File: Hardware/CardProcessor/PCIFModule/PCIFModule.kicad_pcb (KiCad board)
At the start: 8 copper layers, 144 x 70.5 mm, 31 parts, among them J1 MEC5-140-01-L-DV-W1-K, U4 74ABT32, U5 74AHCT04, U6 IDT7381, U8 74ABT16374, U9 74ABT16374

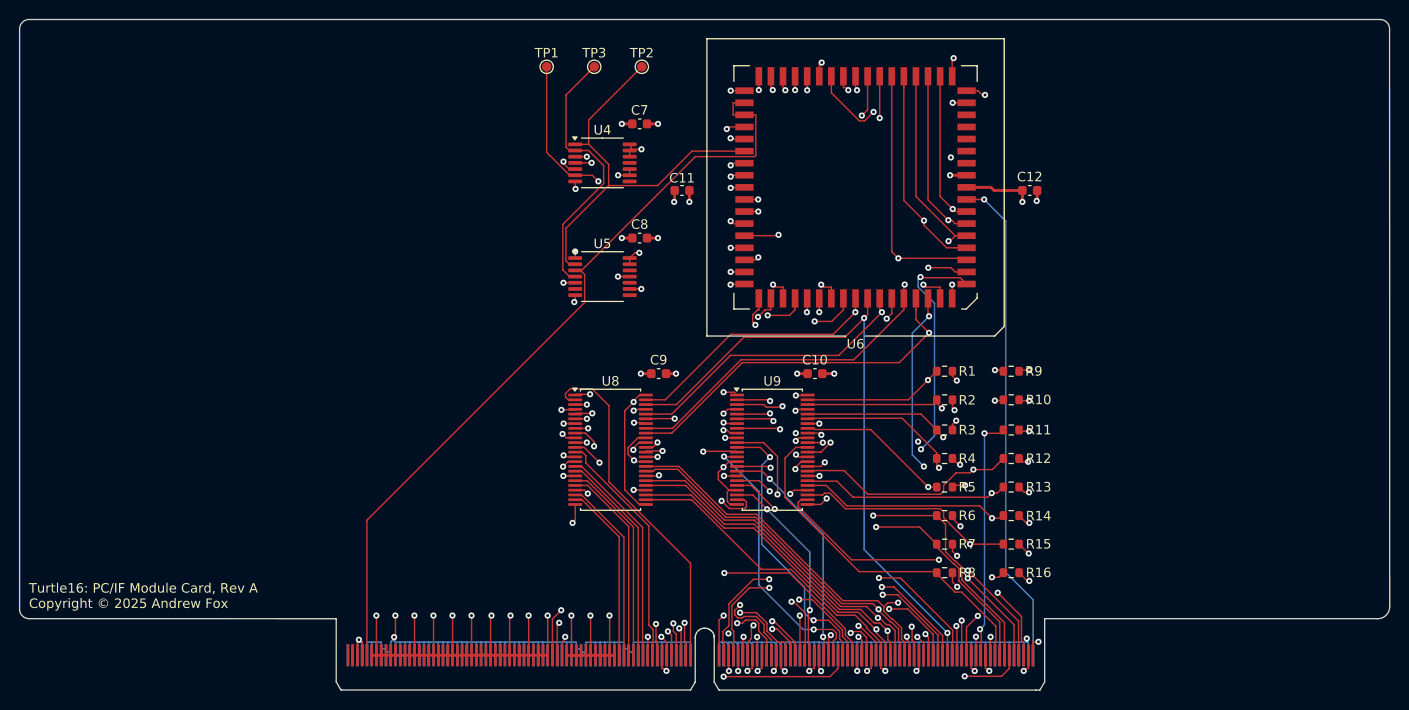
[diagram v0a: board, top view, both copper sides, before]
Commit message: PCIFModule: Route the PCB again, better
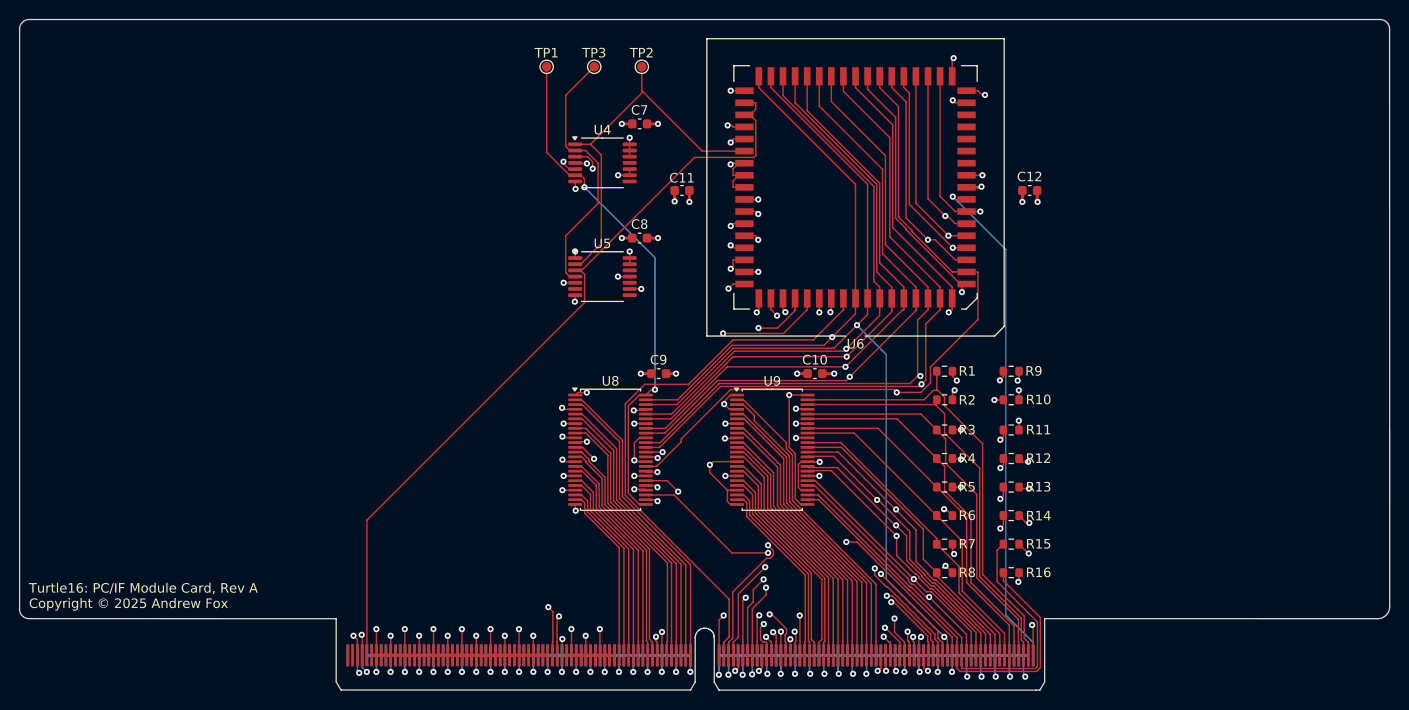
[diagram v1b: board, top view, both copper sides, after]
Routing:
- net GND: track 412.4 -> 314.8 mm, vias 62 -> 104
- net /CardEdgePCIF/Y_EX14: track 70.2 -> 42.7 mm
- net /IF/sheet5FE3DA15/PC5: track 112.5 -> 95.8 mm, vias 3 -> 2
- net /CardEdgePCIF/Ins_ID8: track 41.9 -> 26.2 mm, vias 2 -> 0
- net /CardEdgePCIF/Y_EX15: track 46.1 -> 59.4 mm, vias 2 -> 0
- net /CardEdgePCIF/Ins_IF14: track 35.5 -> 48.6 mm, vias 2 -> 0
- net /CardEdgePCIF/FLUSH_IF: track 96.2 -> 86.7 mm, vias 3 -> 2
- net /CardEdgePCIF/Y_EX3: track 57.4 -> 48.1 mm
- net /CardEdgePCIF/Ins_IF9: track 57.0 -> 48.1 mm, vias 3 -> 2
- net /CardEdgePCIF/Ins_IF15: track 37.2 -> 45.6 mm, vias 3 -> 0
- net /IF/sheet5FE3DA15/PC4: track 103.8 -> 95.6 mm, vias 3 -> 2
- net /CardEdgePCIF/Ins_IF0: track 55.5 -> 47.9 mm, vias 2 -> 0
- net /CardEdgePCIF/Ins_IF4: track 44.0 -> 37.0 mm, vias 2 -> 0
- net /CardEdgePCIF/Y_EX9: track 46.8 -> 39.8 mm
- net /CardEdgePCIF/Ins_ID5: track 35.5 -> 28.8 mm, vias 2 -> 0
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
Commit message: PCIFModule: route the six layer PCB
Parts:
- moved TP2 27.1 mm to (103.2, 63.0)
- moved TP3 23.4 mm to (103.2, 69.0)
- moved TP1 21.4 mm to (103.2, 74.0)
- moved C7 14.0 mm to (116.0, 67.0)
- moved C8 14.0 mm to (116.0, 79.0)
- moved C9 14.0 mm to (118.0, 93.2)
- moved U4 14.0 mm to (112.1, 71.1)
- moved U5 14.0 mm to (112.1, 83.0)
- moved U8 14.0 mm to (112.9, 101.2)
- moved U9 8.46 mm to (135.4, 101.2)
- moved C10 8.46 mm to (139.9, 93.2)
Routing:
- net /CardEdgePCIF/Ins_IF9: track 48.1 -> 77.6 mm, vias 2 -> 0
- net /IF/sheet5FE3DA15/PC9: track 103.5 -> 130.4 mm, vias 3 -> 0
- net /CardEdgePCIF/STALL: track 99.5 -> 124.7 mm, vias 3 -> 2
- net /CardEdgePCIF/FLUSH_IF: track 86.7 -> 111.6 mm
- net Net-(U6-RS1): track 39.9 -> 60.8 mm
- net /IF/sheet5FE3DA15/PC8: track 93.2 -> 111.8 mm, vias 3 -> 2
- net /IF/sheet5FE3DA15/PC4: track 95.6 -> 112.6 mm
- net /CardEdgePCIF/Phi1a: track 94.5 -> 110.9 mm
- net /IF/sheet5FE3DA15/PC5: track 95.8 -> 111.9 mm
- net /CardEdgePCIF/~{J}: track 69.3 -> 85.4 mm, vias 3 -> 2
- net /IF/sheet5FE3DA15/PC2: track 94.8 -> 110.9 mm
- net /IF/sheet5FE3DA15/PC3: track 94.9 -> 110.5 mm
- net /IF/sheet5FE3DA15/PC14: track 95.8 -> 111.2 mm, vias 3 -> 2
- net /CardEdgePCIF/Y_EX15: track 59.4 -> 44.2 mm, vias 0 -> 2
- net /IF/sheet5FE3DA15/PC1: track 95.1 -> 109.6 mm
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- added copper zone on In4.Cu, net GND
- added copper zone on In3.Cu, net VCC
- removed copper zone on In3.Cu, net GND
- removed copper zone on In6.Cu, net GND
- removed copper zone on In4.Cu, net VCC
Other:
- copper layers 8 -> 6
